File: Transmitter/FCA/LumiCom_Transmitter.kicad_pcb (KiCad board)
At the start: 4 copper layers, 50 x 42 mm, 38 parts, among them J1 V, J2 IN_B, J3 IN_A, J4 OUT_B, J5 OUT_A, U1 OPA2675

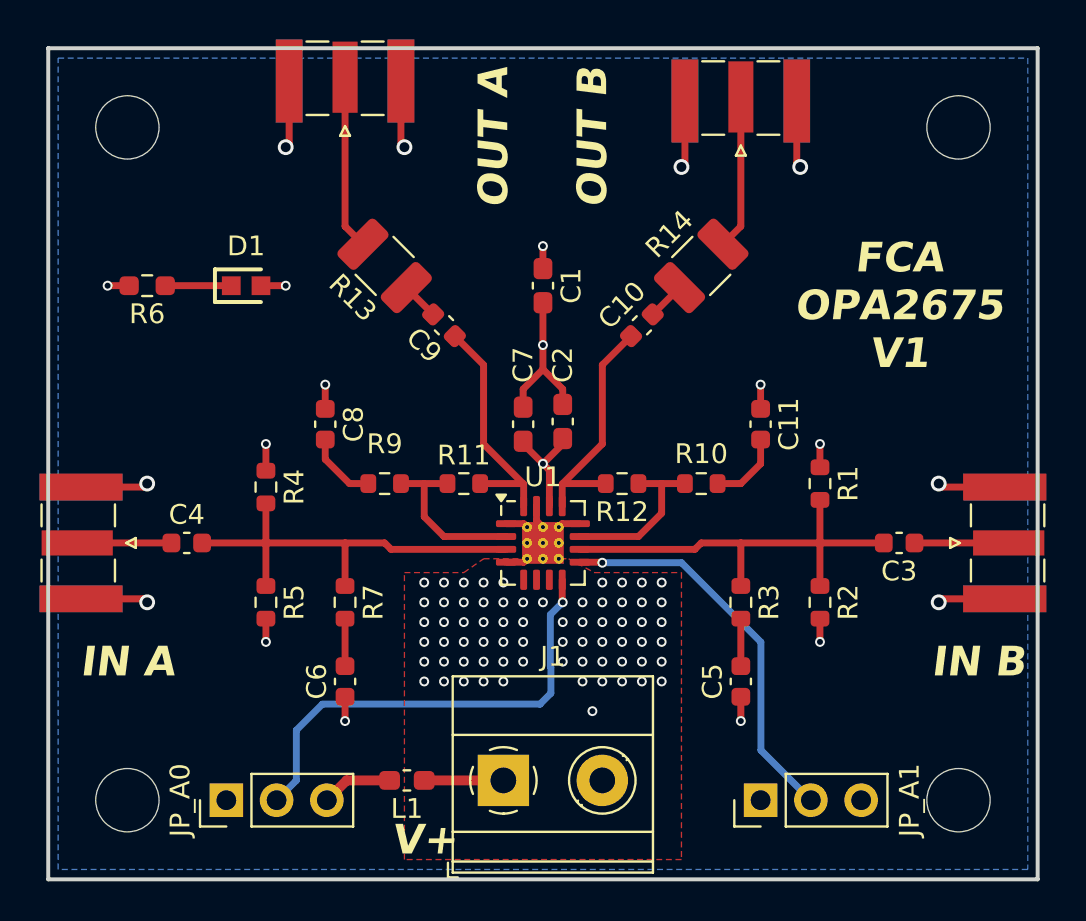
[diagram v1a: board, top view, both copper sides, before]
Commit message: Updated FCA symbols
Updated FCA symbols with mouser number parts.
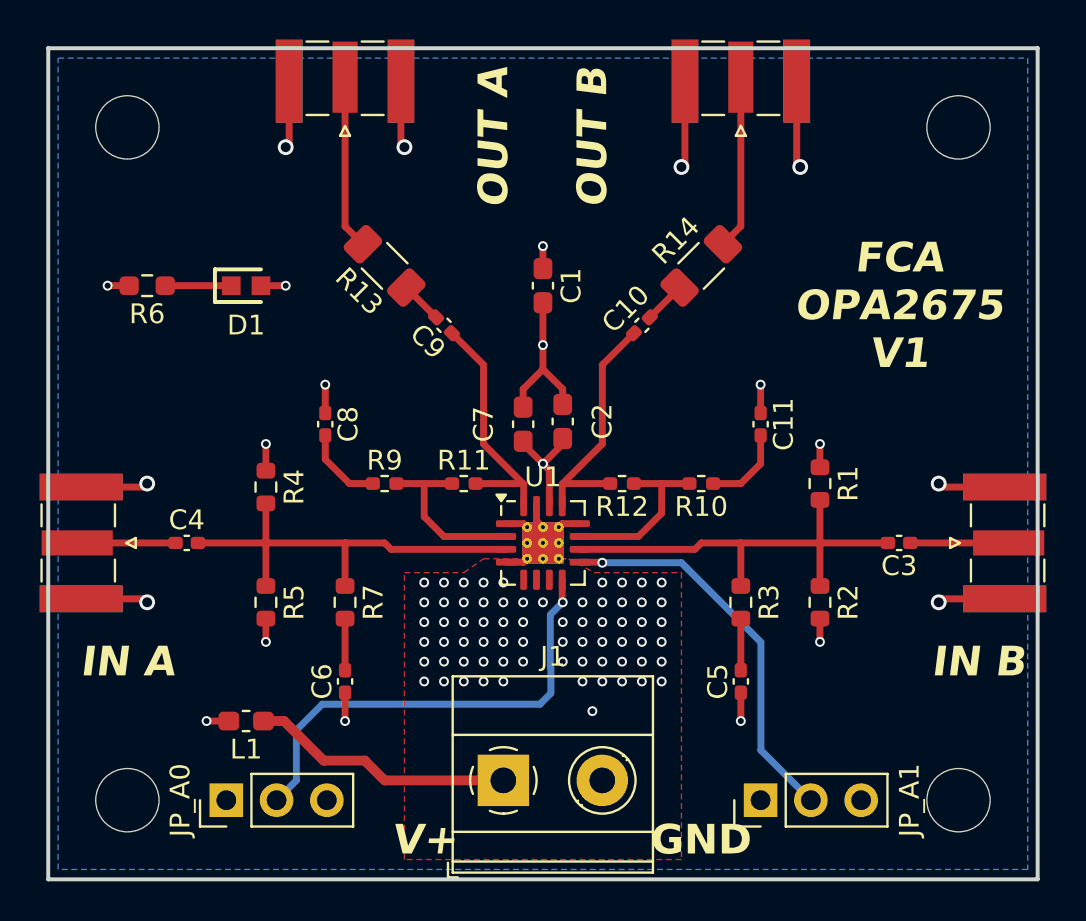
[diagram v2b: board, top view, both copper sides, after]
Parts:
- C10, C11, C3, C4, C5, C6, C8, C9: value 1uF -> .1uF; footprint Capacitor_SMD:C_0603_1608Metric -> Capacitor_SMD:C_0402_1005Metric_Pad0.74x0.62mm_HandSolder
- D1: value 150060VS75000 -> 150060VS75000
- L1: value BLM18BA100SN1D -> Ferrite Beads 220 OHM
- R1, R2: value 5kΩ -> 5.1kΩ
- R10, R9: value 120Ω -> 133Ω; footprint Resistor_SMD:R_0603_1608Metric -> Resistor_SMD:R_0402_1005Metric_Pad0.72x0.64mm_HandSolder
- R11, R12: value 390Ω -> 402Ω; footprint Resistor_SMD:R_0603_1608Metric -> Resistor_SMD:R_0402_1005Metric_Pad0.72x0.64mm_HandSolder
- R13: value 4.3Ω -> 1Ω 1W; footprint Resistor_SMD:R_1210_3225Metric_Pad1.30x2.65mm_HandSolder -> Resistor_SMD:R_1206_3216Metric_Pad1.30x1.75mm_HandSolder
- R14: value 4.3Ω -> 2Ω 1W; footprint Resistor_SMD:R_1210_3225Metric_Pad1.30x2.65mm_HandSolder -> Resistor_SMD:R_1206_3216Metric_Pad1.30x1.75mm_HandSolder
- R3, R7: value 50Ω -> 49.9Ω
- R4, R5: value 1kΩ -> 5.1kΩ
- R6: value 1k2 -> 1k2Ω
- moved L1 8.66 mm to (110.0, 84.0)
- moved J4 1.00 mm to (135.0, 51.7)
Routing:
- net Net-(J1-Pin_1): track 4.00 -> 13.4 mm
- net VCC: track 14.0 -> 11.6 mm, vias 6 -> 7
- net Net-(J4-In): track 7.98 -> 8.82 mm
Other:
- board text added: "GND"

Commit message: FCA DRC fix
FCA DRC fix
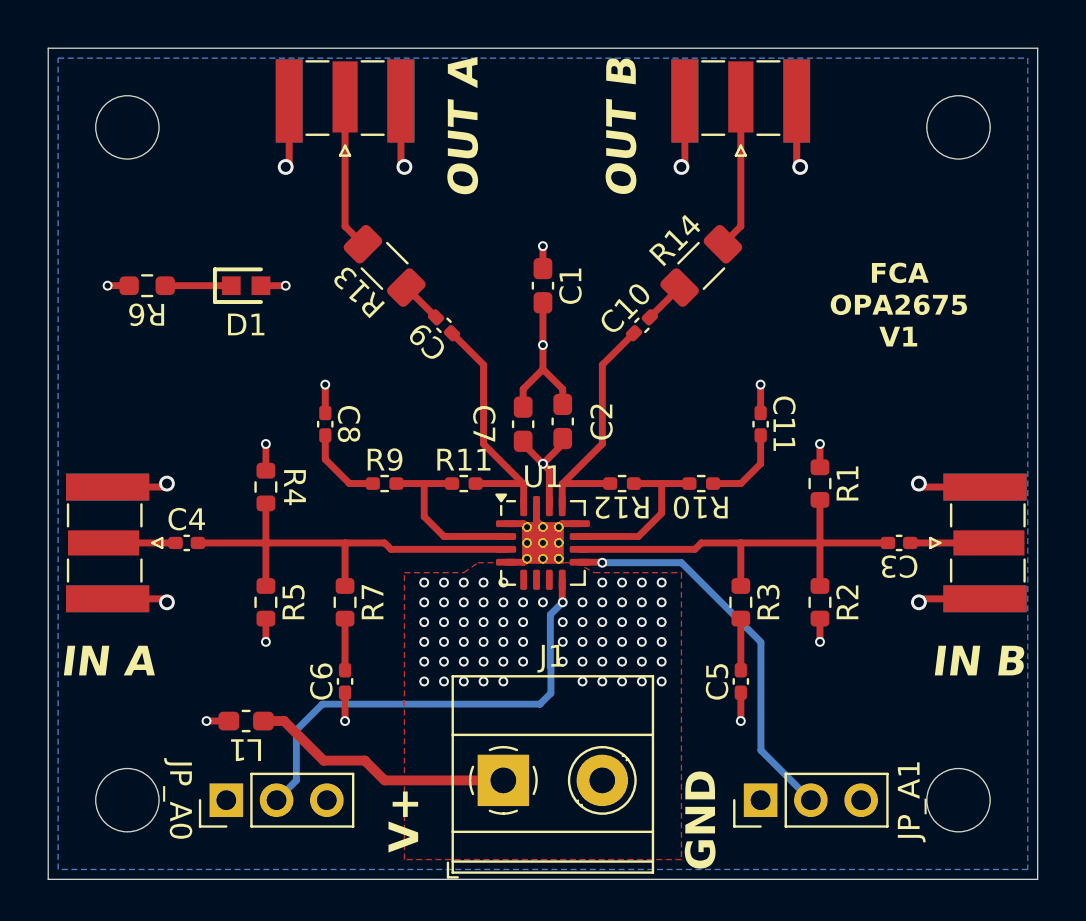
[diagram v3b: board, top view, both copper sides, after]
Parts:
- U1: footprint Package_DFN_QFN:Texas_RGV0016A_VQFN-16-1EP_4x4mm_P0.65mm_EP2.1x2.1mm_ThermalVias -> LumiCom_Transmitter:Texas_OPA2675
- moved J3 1.34 mm to (103.0, 75.0)
- moved J2 1.00 mm to (147.3, 75.0)
- moved J4 1.00 mm to (135.0, 52.7)
- moved J5 1.00 mm to (115.0, 52.7)
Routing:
- net GND: track 48.3 -> 51.6 mm
- net VCC: vias 7 -> 6
